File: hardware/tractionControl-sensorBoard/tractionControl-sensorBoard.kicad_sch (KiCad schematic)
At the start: 3 parts, among them IC1 LTC6820_MSOP, U1 TLE5012B, U2 ATtiny4313-P

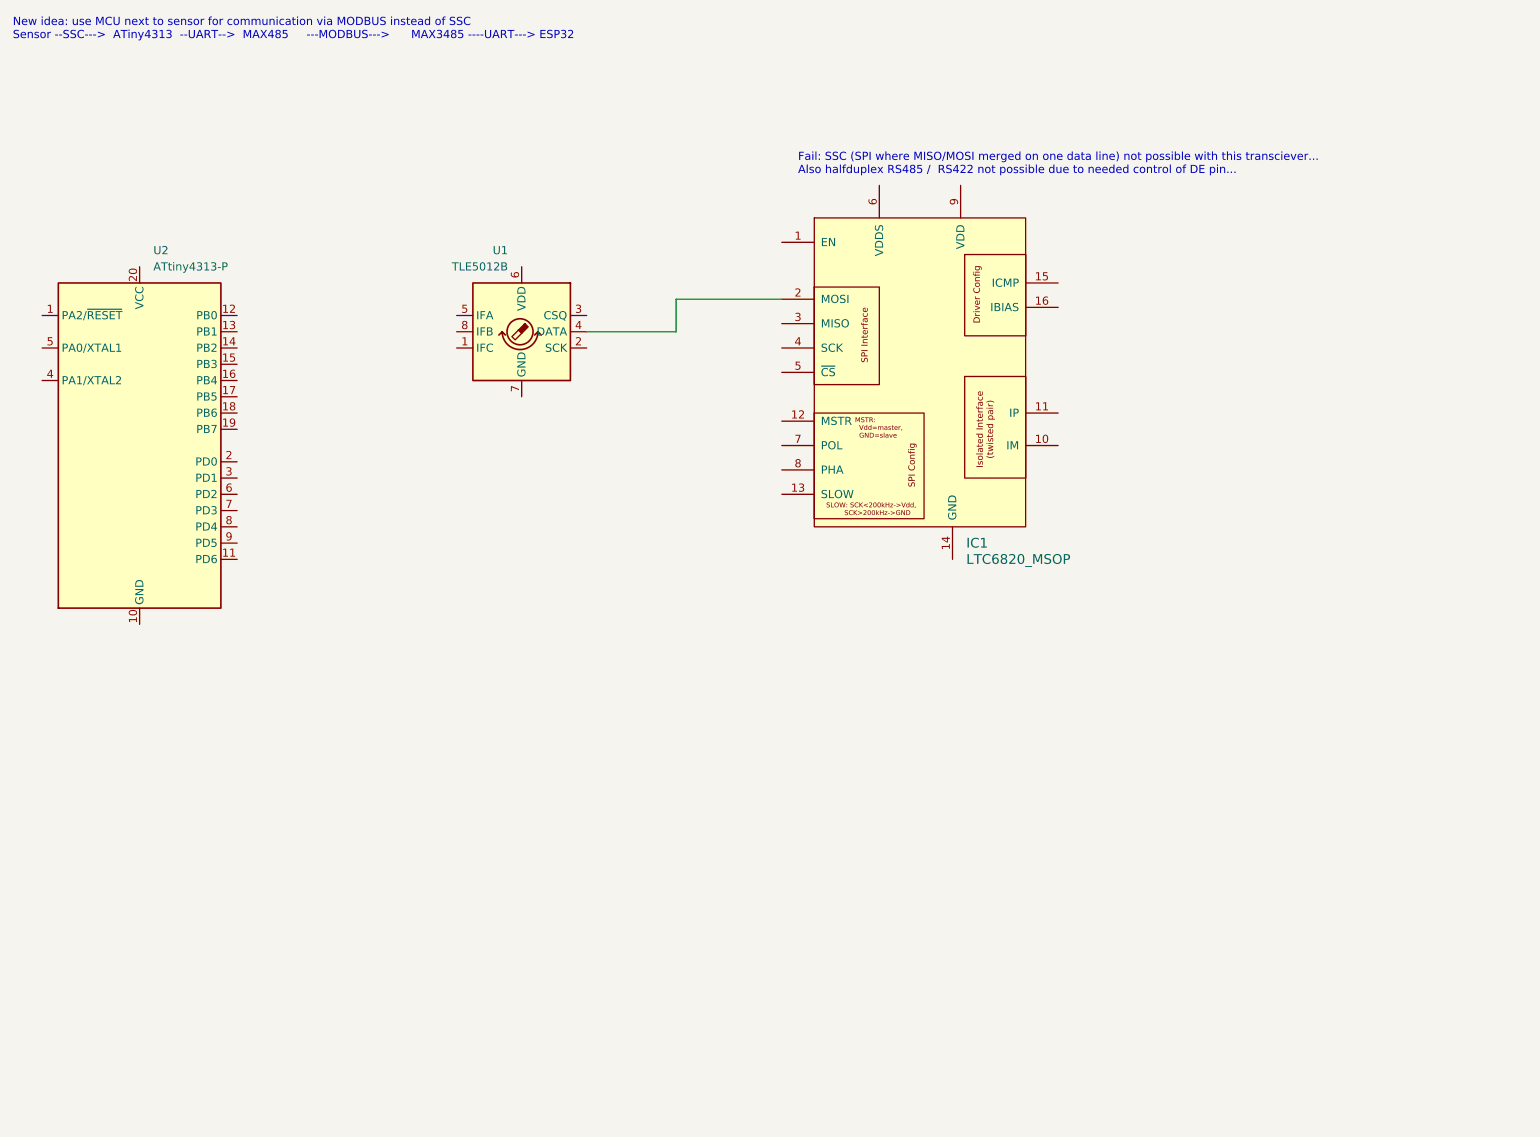
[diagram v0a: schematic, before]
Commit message: Add notes about found sensor/tranciever ics
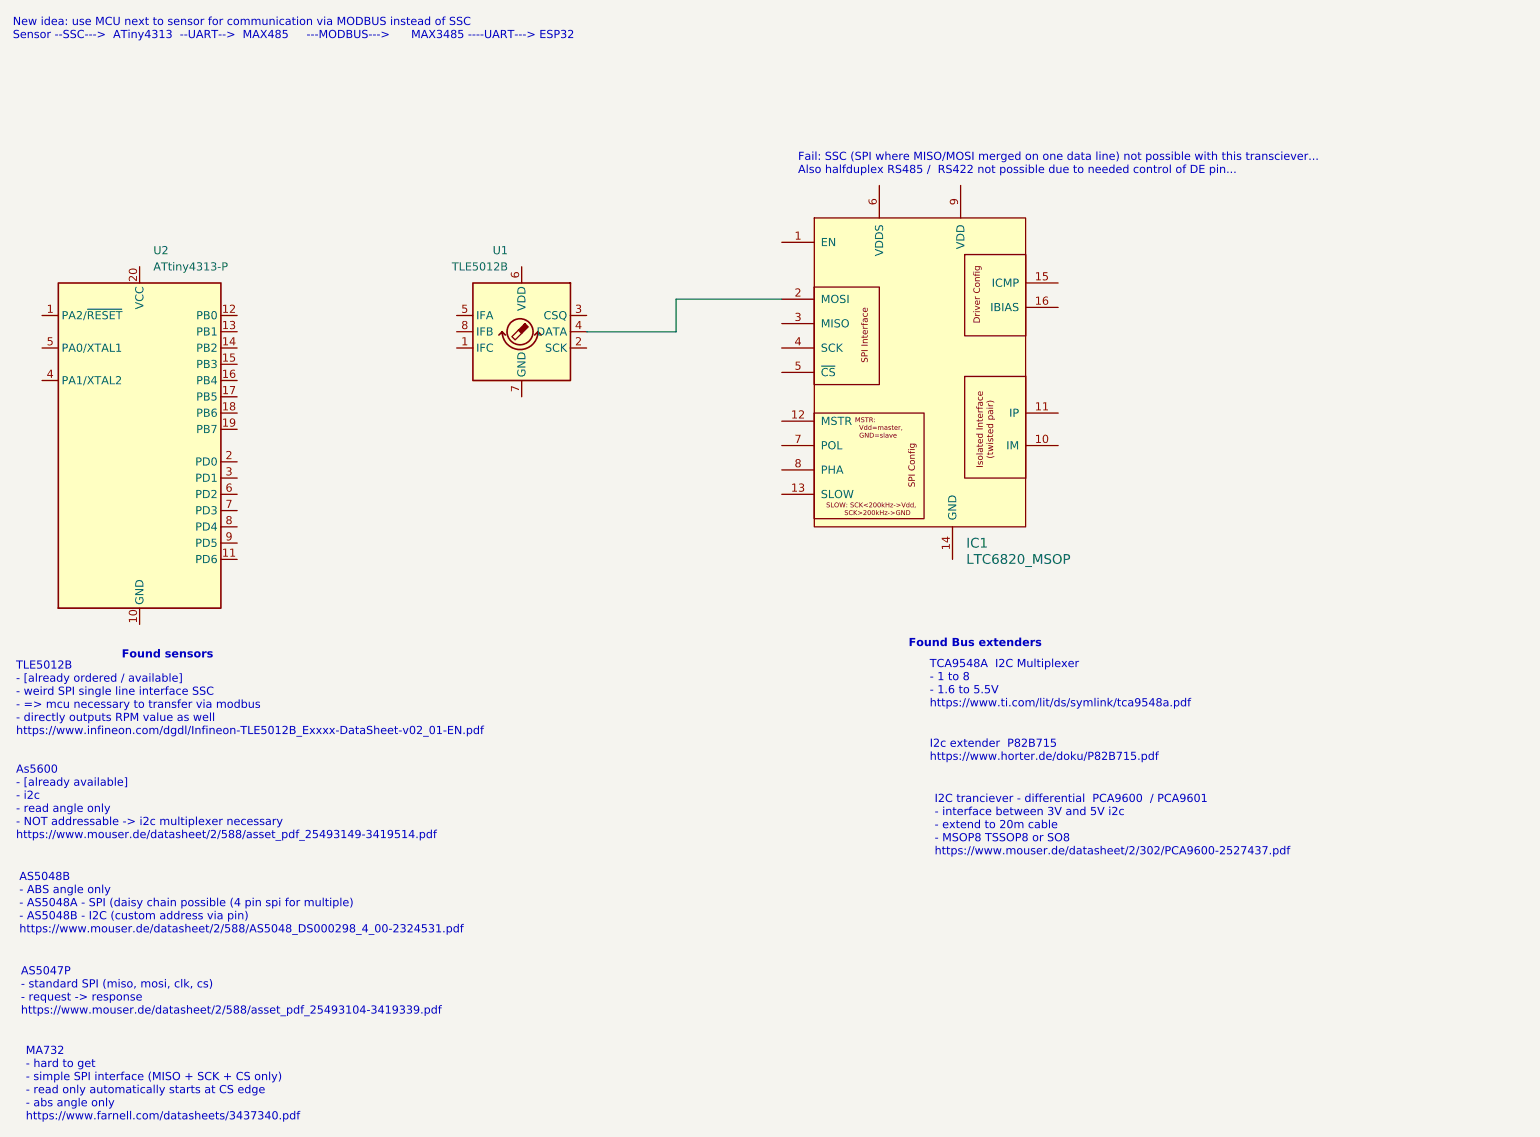
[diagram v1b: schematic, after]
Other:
- note added: "AS5047P - standard SPI (miso, mosi, clk, cs) - request -> response https://www.mouser.de/datasheet/2/588/asset_pdf_25493104-3419339.pdf"
- note added: "AS5048B - ABS angle only - AS5048A - SPI (daisy chain possible (4 pin spi for multiple) - AS5048B - I2C (custom address via pin) https://www.mouser.de/datasheet/2/588/AS5048_DS000298_4_00-2324531.pdf"
- note added: "As5600 - [already available] - i2c - read angle only - NOT addressable -> i2c multiplexer necessary https://www.mouser.de/datasheet/2/588/asset_pdf_25493149-3419514.pdf"
- note added: "Found Bus extenders"
- note added: "Found sensors"
- note added: "I2C tranciever - differential PCA9600 / PCA9601 - interface between 3V and 5V i2c - extend to 20m cable - MSOP8 TSSOP8 or SO8 https://www.mouser.de/datasheet/2/302/PCA9600-2527437.pdf"
- note added: "I2c extender P82B715 https://www.horter.de/doku/P82B715.pdf"
- note added: "MA732 - hard to get - simple SPI interface (MISO + SCK + CS only) - read only automatically starts at CS edge - abs angle only https://www.farnell.com/datasheets/3437340.pdf"
- note added: "TCA9548A I2C Multiplexer - 1 to 8 - 1.6 to 5.5V https://www.ti.com/lit/ds/symlink/tca9548a.pdf"
- note added: "TLE5012B - [already ordered / available] - weird SPI single line interface SSC - => mcu necessary to transfer via modbus - directly outputs RPM value as well https://www.infineon.com/dgdl/Infineon-TLE5012B_Exxxx-DataSheet-v02_01-EN.pdf"
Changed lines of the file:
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@@
 	(generator_version "9.0")
 	(paper "A4")
+	(text "MA732\n- hard to get\n- simple SPI interface (MISO + SCK + CS only)\n- read only automatically starts at CS edge\n- abs angle only\nhttps://www.farnell.com/datasheets/3437340.pdf"
+		(exclude_from_sim no)
+		(at 27.94 187.452 0)
+		(effects
+			(font
+				(size 1.27 1.27)
+			)
+			(justify left)
+		)
+	)
+	(text "As5600\n- [already available]\n- i2c \n- read angle only\n- NOT addressable -> i2c multiplexer necessary\nhttps://www.mouser.de/datasheet/2/588/asset_pdf_25493149-3419514.pdf"
+		(exclude_from_sim no)
+		(at 26.416 143.51 0)
+		(effects
+			(font
+				(size 1.27 1.27)
+			)
+			(justify left)
+		)
+	)
 	(text "New idea: use MCU next to sensor for communication via MODBUS instead of SSC\nSensor --SSC--->  ATiny4313  --UART-->  MAX485     ---MODBUS--->      MAX3485 ----UART---> ESP32"
 		(exclude_from_sim no)
 		(at 25.908 22.606 0)
+		(effects
+			(font
+				(size 1.27 1.27)
+			)
+			(justify left)
+		)
+	)
+	(text "I2c extender  P82B715\nhttps://www.horter.de/doku/P82B715.pdf"
+		(exclude_from_sim no)
+		(at 169.164 135.382 0)
+		(effects
+			(font
+				(size 1.27 1.27)
+				(thickness 0.1588)
+			)
+			(justify left)
+		)
+	)
+	(text "AS5047P\n- standard SPI (miso, mosi, clk, cs)\n- request -> response\nhttps://www.mouser.de/datasheet/2/588/asset_pdf_25493104-3419339.pdf"
+		(exclude_from_sim no)
+		(at 27.178 172.974 0)
 		(effects
 			(font
@@
 			)
 			(justify left)
+		)
+	)
+	(text "AS5048B\n- ABS angle only\n- AS5048A - SPI (daisy chain possible (4 pin spi for multiple)\n- AS5048B - I2C (custom address via pin)\nhttps://www.mouser.de/datasheet/2/588/AS5048_DS000298_4_00-2324531.pdf"
+		(exclude_from_sim no)
+		(at 26.924 159.258 0)
+		(effects
+			(font
+				(size 1.27 1.27)
+			)
+			(justify left)
+		)
+	)
+	(text "I2C tranciever - differential  PCA9600  / PCA9601\n- interface between 3V and 5V i2c\n- extend to 20m cable\n- MSOP8 TSSOP8 or SO8\nhttps://www.mouser.de/datasheet/2/302/PCA9600-2527437.pdf"
+		(exclude_from_sim no)
+		(at 169.926 147.066 0)
+		(effects
+			(font
+				(size 1.27 1.27)
+				(thickness 0.1588)
+			)
+			(justify left)
+		)
+	)
+	(text "TLE5012B\n- [already ordered / available]\n- weird SPI single line interface SSC\n- => mcu necessary to transfer via modbus\n- directly outputs RPM value as well\nhttps://www.infineon.com/dgdl/Infineon-TLE5012B_Exxxx-DataSheet-v02_01-EN.pdf"
+		(exclude_from_sim no)
+		(at 26.416 127.254 0)
+		(effects
+			(font
+				(size 1.27 1.27)
+			)
+			(justify left)
+		)
+	)
+	(text "TCA9548A  I2C Multiplexer\n- 1 to 8\n- 1.6 to 5.5V\nhttps://www.ti.com/lit/ds/symlink/tca9548a.pdf"
+		(exclude_from_sim no)
+		(at 169.164 124.968 0)
+		(effects
+			(font
+				(size 1.27 1.27)
+			)
+			(justify left)
+		)
+	)
+	(text "Found sensors"
+		(exclude_from_sim no)
+		(at 42.926 120.396 0)
+		(effects
+			(font
+				(size 1.27 1.27)
+				(thickness 0.254)
+				(bold yes)
+			)
+			(justify left)
+		)
+	)
+	(text "Found Bus extenders"
+		(exclude_from_sim no)
+		(at 165.862 118.618 0)
+		(effects
+			(font
+				(size 1.27 1.27)
+				(thickness 0.254)
+				(bold yes)
+			)
+			(justify left)
